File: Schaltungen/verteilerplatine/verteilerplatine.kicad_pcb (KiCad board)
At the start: 2 copper layers, 20 parts, among them P1 DIN_5, T1 MOSFET_N, T2 MOSFET_N, T3 NPN, T4 PNP

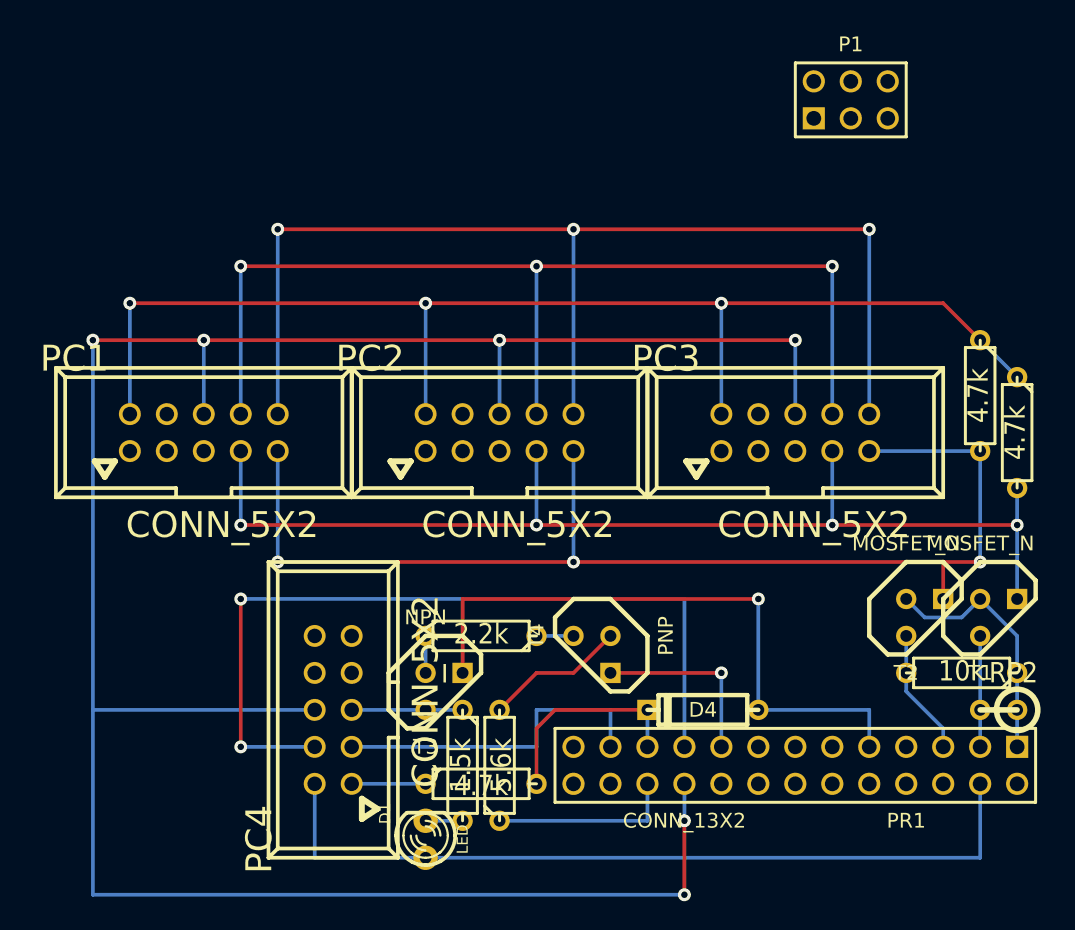
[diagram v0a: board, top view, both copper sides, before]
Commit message: Anpassung der Verteiler-Platine (Verbindung der Trigger-Leitung)
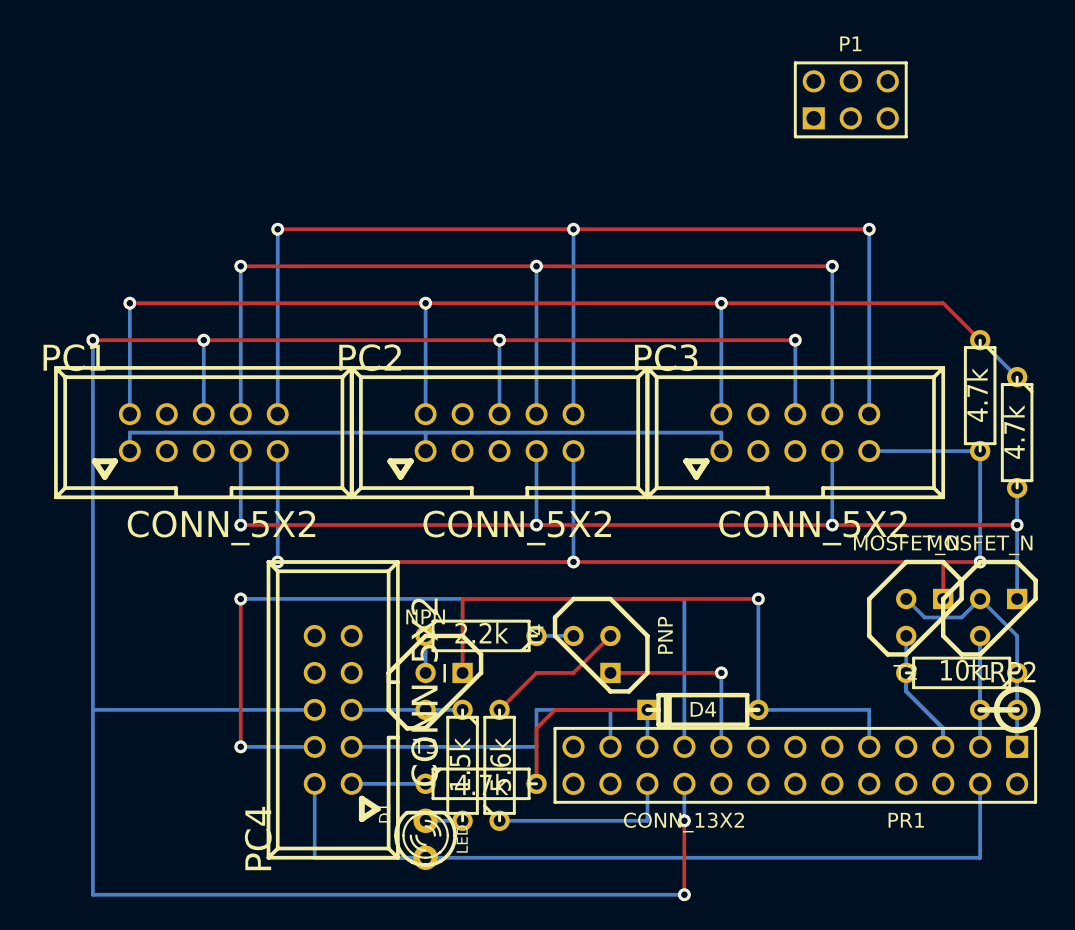
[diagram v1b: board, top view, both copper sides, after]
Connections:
- PC1 pad 1: (no net) -> N-0000026
- PC2 pad 1: (no net) -> N-0000026
- PC3 pad 1: (no net) -> N-0000026
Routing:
- net N-0000026: track 0.00 -> 44.5 mm
- net +5V: track 141.8 -> 149.4 mm
- net /RaspberryPI/SCL: track 8.67 -> 14.8 mm
- net /RaspberryPI/SDA: track 7.62 -> 12.7 mm
